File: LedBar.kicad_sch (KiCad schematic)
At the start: 35 parts, among them U1 74AHC04, U2 74AHC04, U3 74AHC04

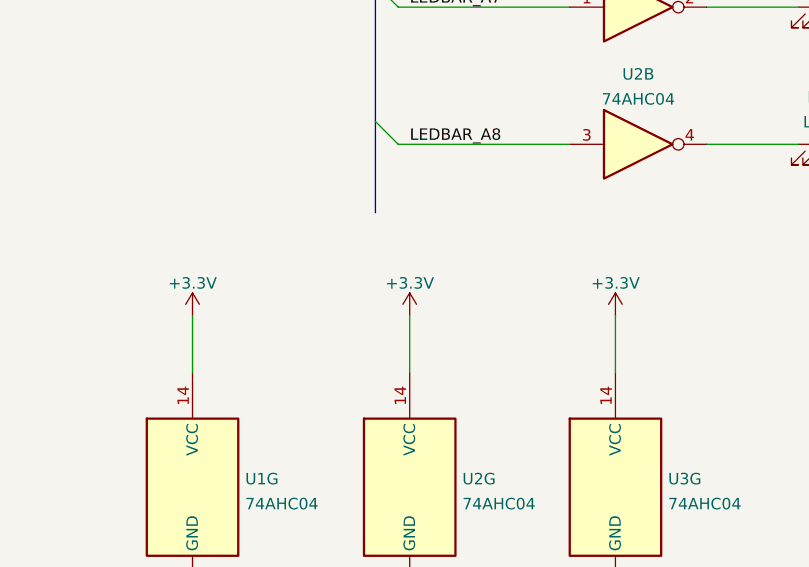
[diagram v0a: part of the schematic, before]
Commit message: Atualizados os Footprints. Definido um primeiro corte da placa.
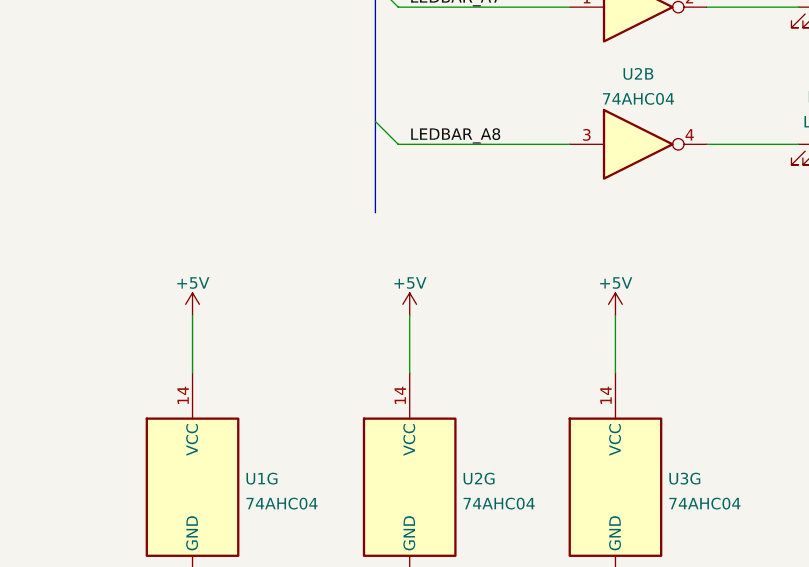
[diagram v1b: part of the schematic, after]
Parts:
- R1, R10, R11, R12, R13, R14, R15, R16, R2, R3, R4, R5, R6, R7, R8, R9: footprint Resistor_THT:R_Axial_DIN0204_L3.6mm_D1.6mm_P5.08mm_Horizontal -> Resistor_THT:R_Axial_DIN0207_L6.3mm_D2.5mm_P7.62mm_Horizontal
- U1, U2, U3: footprint Package_DIP:DIP-14_W7.62mm_Socket -> Package_DIP:DIP-14_W7.62mm
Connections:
- net +3V3 is gone; now on net +5V: U1.14 (VCC), U2.14 (VCC), U3.14 (VCC)

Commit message: Placa roeada automaticamente.
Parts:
- added C1, C2, C3: 10uF, Capacitor_THT:CP_Radial_D5.0mm_P2.50mm, symbol Device:C_Polarized
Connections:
- net +5V: now also C1.1, C2.1, C3.1
- net GND: now also C1.2, C2.2, C3.2
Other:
- company: (none) -> IFTM - Campus Ituiutaba
- title: (none) -> FPGA LED Output Board - LEDs
- moved on the sheet: U1G, U2G, U3G
